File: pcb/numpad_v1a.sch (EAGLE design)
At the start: 86 parts, among them IC1 ATMEGA32U4-MU, IC2 IS31FL3731-SALS2, SW1 EVQP2, X1 16MHz

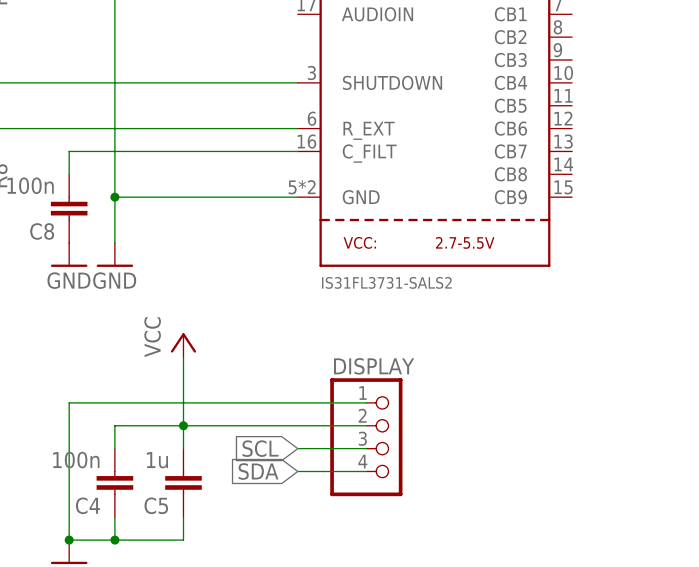
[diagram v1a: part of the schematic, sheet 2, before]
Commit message: fix(schematic): Corrected LED driver part number
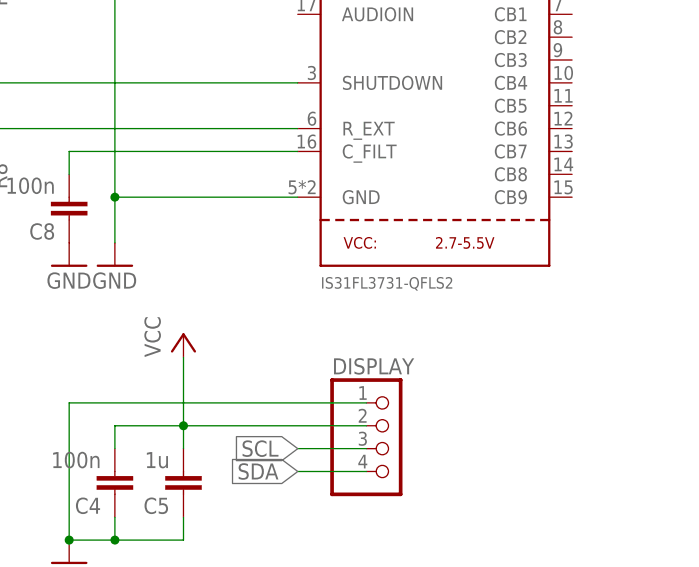
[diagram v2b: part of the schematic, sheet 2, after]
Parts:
- IC2: value IS31FL3731-SALS2 -> IS31FL3731-QFLS2
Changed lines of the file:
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@@
 <attribute name="LCSC" value="C81598"/>
 </part>
-<part name="IC2" library="microbuilder" deviceset="IS31FL3731" device="QFN" value="IS31FL3731-SALS2"/>
+<part name="IC2" library="microbuilder" deviceset="IS31FL3731" device="QFN" value="IS31FL3731-QFLS2"/>
 <part name="GND8" library="supply1" library_urn="urn:adsk.eagle:library:371" deviceset="GND" device=""/>
 <part name="P+4" library="supply1" library_urn="urn:adsk.eagle:library:371" deviceset="VCC" device=""/>
